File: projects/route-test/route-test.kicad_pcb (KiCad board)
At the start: 2 copper layers, 30 x 20 mm, 3 parts, among them J1 Conn_01x03

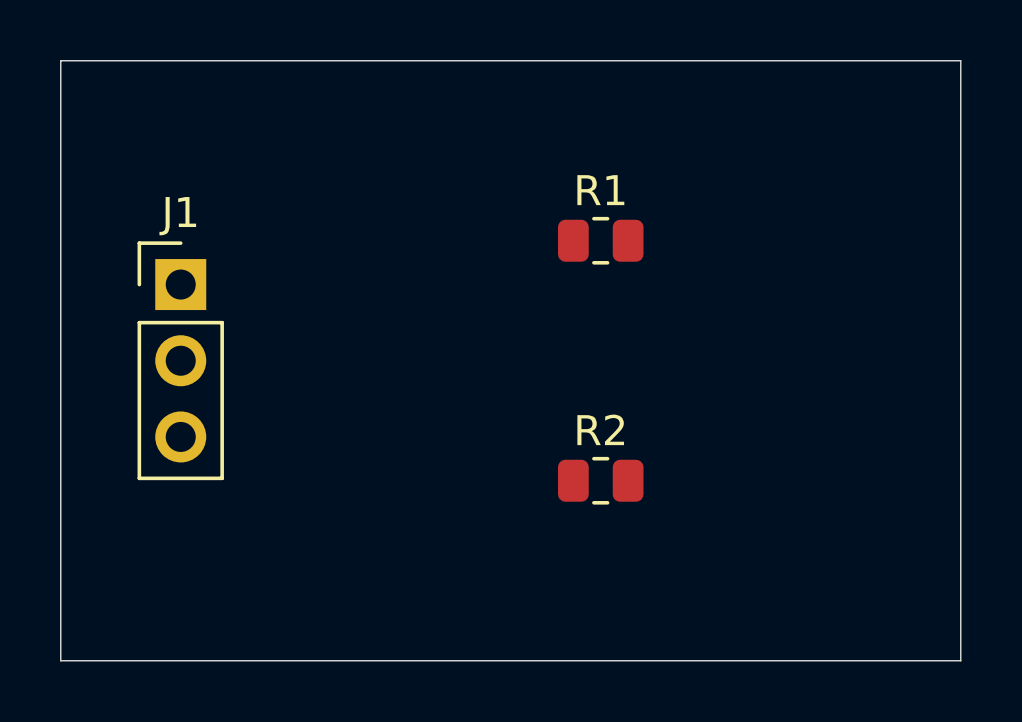
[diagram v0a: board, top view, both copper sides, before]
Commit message: route-test: replace R1/R2 with THT footprints on board and place
Konnect's schematic sync refuses footprint_id changes, so R1/R2 were deleted
via IPC and re-added by update_pcb_from_schematic.

Co-Authored-By: Claude Opus 5.5 <noreply@anthropic.com>
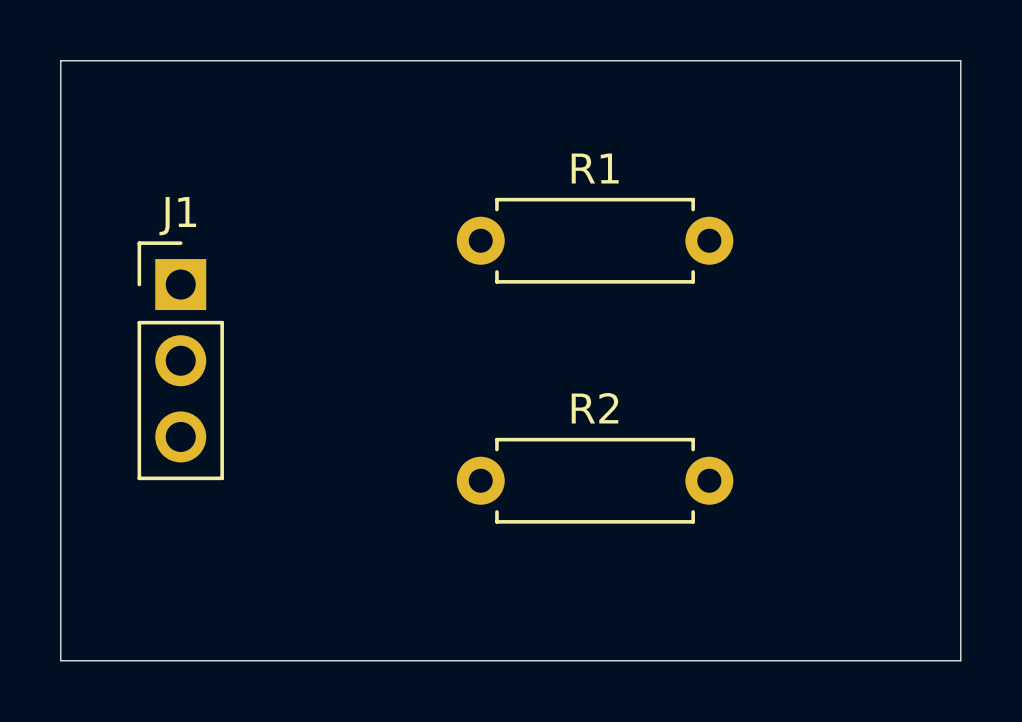
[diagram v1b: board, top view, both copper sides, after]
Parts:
- R1, R2: footprint Resistor_SMD:R_0805_2012Metric -> Resistor_THT:R_Axial_DIN0207_L6.3mm_D2.5mm_P7.62mm_Horizontal
- moved R1 4.00 mm to (114.0, 106.0)
- moved R2 4.00 mm to (114.0, 114.0)
